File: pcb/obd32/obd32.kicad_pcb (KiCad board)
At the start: 2 copper layers, 49.5 x 48.8 mm, 58 parts, among them J1 USB_C_Receptacle_USB2.0, J2 Micro_SD_Card, J3 OBD2, J4 67329-8040, J5 Conn_01x04_Female, SW1 SW_Push, SW2 SW_Push, U1 LMR33630BDDA, U2 ICM-20689, U3 AZ1117C-3.3, U4 ESP32-WROOM-32, U5 SiP32431DR3, U6 MCP2562-E-MF, U7 BMP280, U8 CP2102N-A01-GQFN24

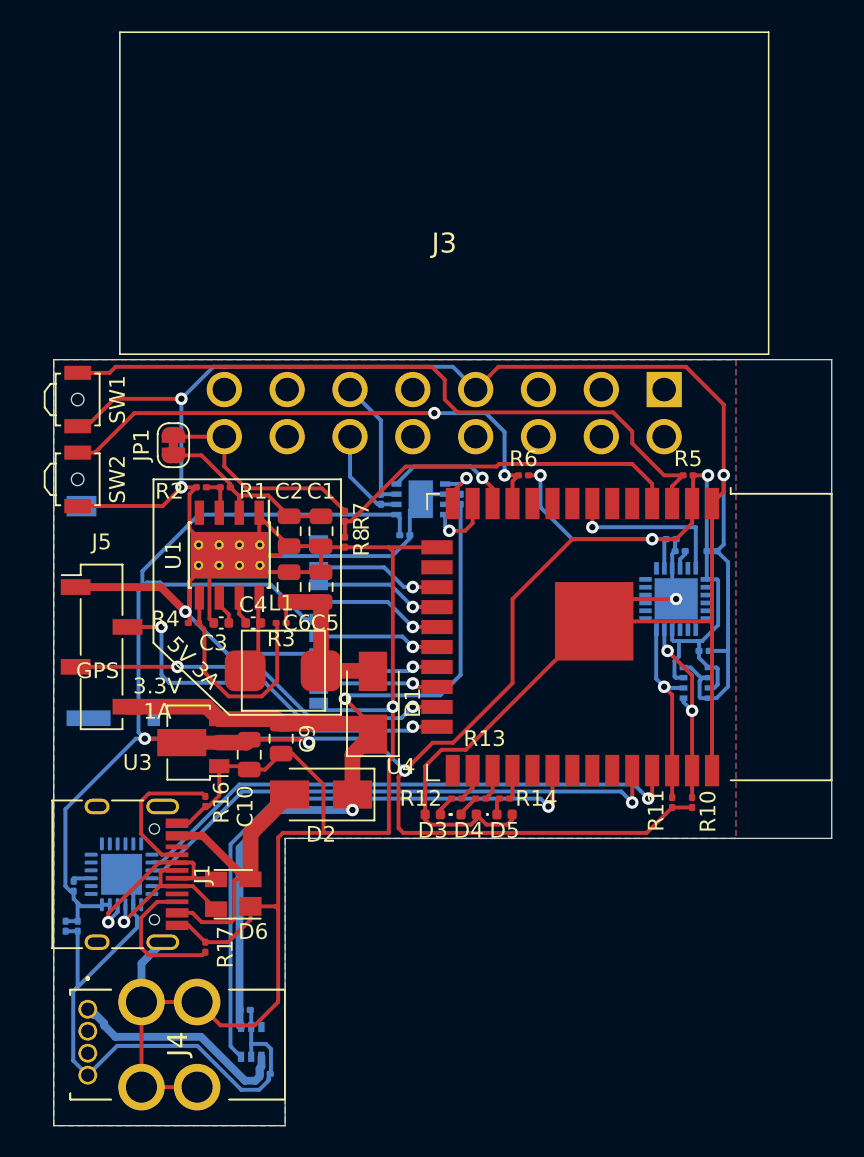
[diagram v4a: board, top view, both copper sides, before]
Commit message: Board: some refinement; Add button BOOT0
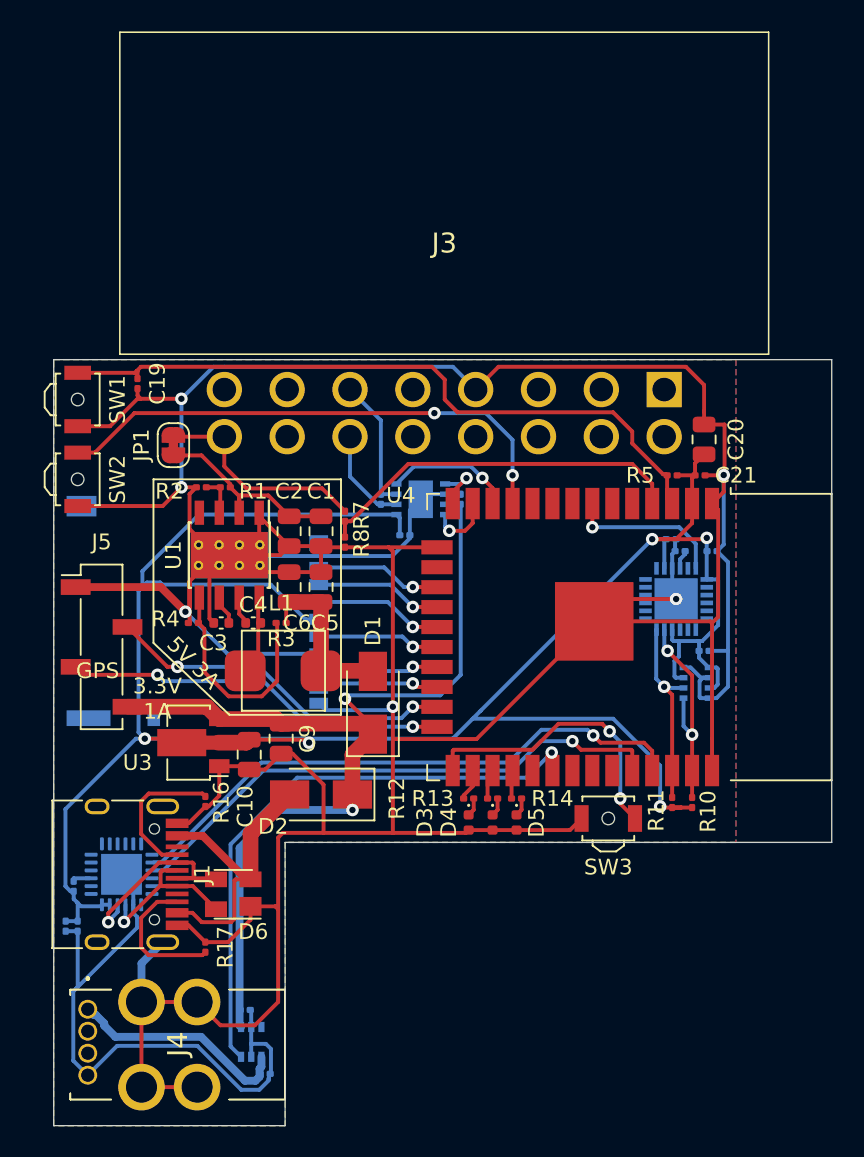
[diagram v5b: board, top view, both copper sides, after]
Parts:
- removed R6: 100K, Resistor_SMD:R_0201_0603Metric
- added C19: 1µF, Capacitor_SMD:C_0201_0603Metric, F.Cu at (202.2, 63.8)
- added C20: 10µF, Capacitor_SMD:C_0805_2012Metric, F.Cu at (238.3, 67.3)
- added C21: 0.1µF, Capacitor_SMD:C_0201_0603Metric, F.Cu at (238.0, 69.6)
- added SW3: SW_Push, Button_Switch_SMD:SW_SPST_B3U-3000P-B, F.Cu at (232.2, 91.4)
- R5: value 100K -> 10K
- moved D3 2.34 mm to (223.3, 91.7), turned to 270 degrees
- moved D4 1.61 mm to (224.8, 91.7), turned to 270 degrees
- moved R5 1.02 mm to (236.2, 69.6)
- moved D5 0.92 mm to (226.3, 91.7), turned to 270 degrees
- moved R12 0.76 mm to (223.3, 90.2), turned to 180 degrees
- moved R13 0.76 mm to (224.8, 90.2), turned to 180 degrees
- moved R14 0.76 mm to (226.3, 90.2), turned to 180 degrees
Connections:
- net Net-(R7-Pad2) renamed ADC
- J5 pad 2: GPS_TX -> GPS_RX
- J5 pad 3: GPS_RX -> GPS_TX
- U4 pad 25: (no net) -> BOOT0
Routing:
- net +3V3: track 178.8 -> 159.7 mm, vias 6 -> 5
- net BOOT0: track 0.00 -> 18.4 mm, vias 0 -> 2
- net GND: track 353.4 -> 360.1 mm
- net GPS_RX: track 24.7 -> 22.4 mm
- net I2C0_SCL: track 12.4 -> 14.0 mm
- net UART_TX: track 35.8 -> 37.1 mm
- net ESP32_MISC: track 34.3 -> 33.5 mm
- net ESP32_EN: track 44.8 -> 44.2 mm
- net IMU_INT: track 10.7 -> 10.1 mm
- net UART_RX: track 34.9 -> 35.4 mm
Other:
- outline, holes or cut-outs redrawn
